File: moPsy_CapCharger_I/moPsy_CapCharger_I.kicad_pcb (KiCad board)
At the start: 2 copper layers, 30 x 31 mm, 12 parts, among them J1 Conn_01x08_Male, U1 LM79L12_TO92, U2 LM555xN

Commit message: Add OSHW logo to Cap Charger PCB
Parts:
- added REF**: OSHW-Logo2_7.3x6mm_SilkScreen, Symbol:OSHW-Logo2_7.3x6mm_SilkScreen, B.Cu at (104.8, 67.3)

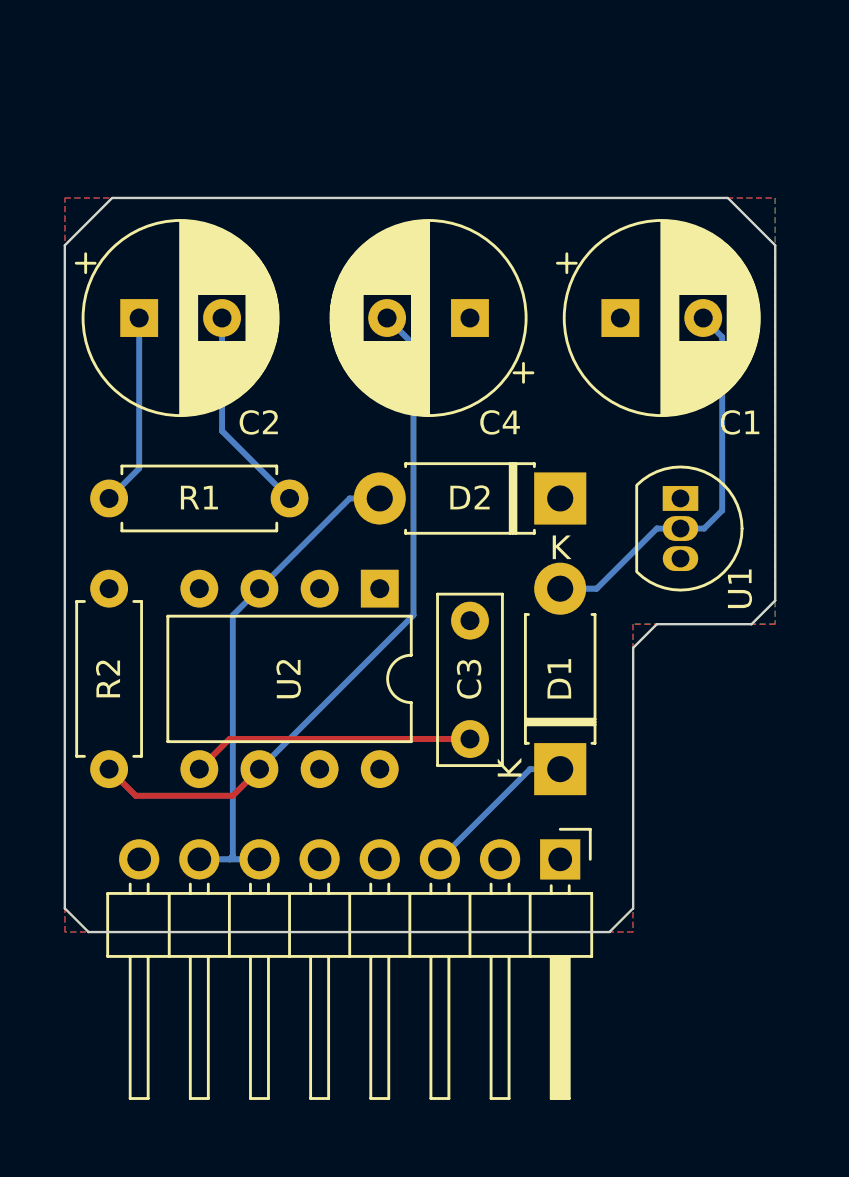
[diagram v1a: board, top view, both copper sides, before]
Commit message: Design a new PCB for the cap charger
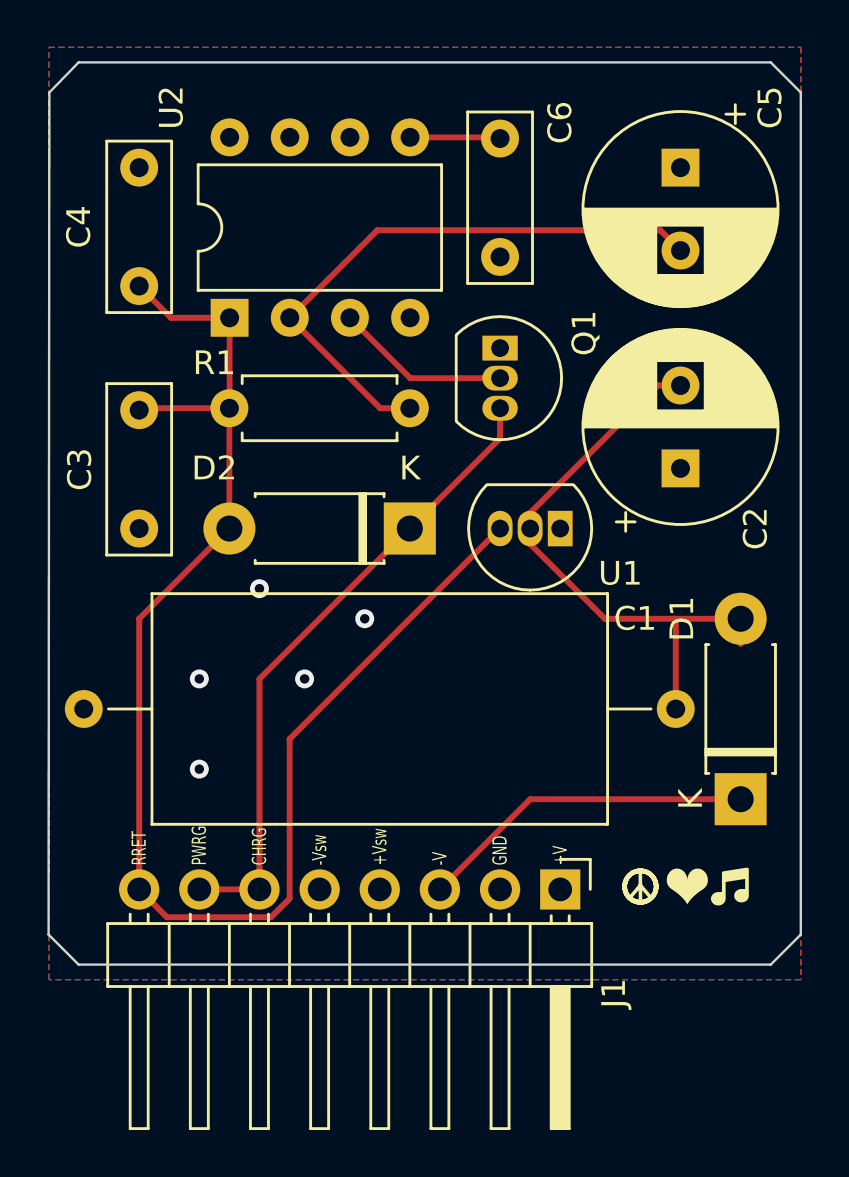
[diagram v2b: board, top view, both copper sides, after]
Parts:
- removed R2: 47k, Resistor_THT:R_Axial_DIN0207_L6.3mm_D2.5mm_P7.62mm_Horizontal
- removed REF**: OSHW-Logo2_7.3x6mm_SilkScreen, Symbol:OSHW-Logo2_7.3x6mm_SilkScreen
- added C5: 100u, Capacitor_THT:CP_Radial_D8.0mm_P3.50mm, F.Cu at (127.0, 45.7)
- added C6: 10n, Capacitor_THT:C_Rect_L7.0mm_W2.5mm_P5.00mm, F.Cu at (119.4, 49.5)
- added Q1: BC547, Package_TO_SOT_THT:TO-92_Inline, F.Cu at (119.4, 53.3)
- C1: value 33u -> 470u; footprint Capacitor_THT:CP_Radial_D8.0mm_P3.50mm -> Capacitor_THT:C_Axial_L19.0mm_D9.5mm_P25.00mm_Horizontal
- C2: value 100n -> 33u
- C3: value 10n -> 100n
- C4: value 100u -> 100n; footprint Capacitor_THT:CP_Radial_D8.0mm_P3.50mm -> Capacitor_THT:C_Rect_L7.0mm_W2.5mm_P5.00mm
- R1: value 10k -> 47k
- moved C1 28.0 mm to (101.8, 68.6)
- moved C2 23.7 mm to (127.0, 58.4), turned to 90 degrees
- moved C3 16.6 mm to (104.1, 61.0)
- moved C4 15.3 mm to (104.1, 45.7), turned to -90 degrees
- moved Ref** 13.8 mm to (113.7, 68.6)
- moved R1 13.3 mm to (115.6, 55.9), turned to 180 degrees
- moved U2 13.1 mm to (108.0, 52.1), turned to 90 degrees
- moved D1 7.73 mm to (129.5, 72.4)
- moved D2 6.48 mm to (115.6, 61.0)
- moved U1 5.24 mm to (121.9, 61.0), turned to 180 degrees
- moved J1 1.27 mm to (121.9, 76.2)
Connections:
- C1 pad 1: REL_RETURN -> GND
- C1 pad 2: Net-(C1-Pad2) -> Net-(C2-Pad2)
- C2 pad 1: REL_RETURN -> GND
- C2 pad 2: -12V -> Net-(C2-Pad2)
- C3 pad 1: Net-(C3-Pad1) -> GND
- C3 pad 2: -12V -> REL_RETURN
- C4 pad 1: REL_RETURN -> GND
- C4 pad 2: Net-(C4-Pad2) -> REL_RETURN
- D1 pad 2: Net-(C1-Pad2) -> Net-(C2-Pad2)
- D2 pad 1: REL_RETURN -> REL_Charge
- D2 pad 2: REL_Charge -> REL_RETURN
- J1 pad 1: (no net) -> +15V
- J1 pad 2: REL_RETURN -> GND
- J1 pad 4: (no net) -> +15V_SW
- J1 pad 5: (no net) -> -15V_SW
- R1 pad 1: REL_RETURN -> Net-(C5-Pad2)
- R1 pad 2: -12V -> REL_RETURN
- U1 pad 1: REL_RETURN -> GND
- U1 pad 2: Net-(C1-Pad2) -> Net-(C2-Pad2)
- U1 pad 3: -12V -> REL_RETURN
- U2 pad 1: -12V -> REL_RETURN
- U2 pad 2: -12V -> Net-(C5-Pad2)
- U2 pad 3: REL_Charge -> Net-(U2-Pad3)
- U2 pad 4: REL_RETURN -> GND
- U2 pad 5: Net-(C3-Pad1) -> Net-(U2-Pad5)
- U2 pad 6: Net-(C4-Pad2) -> unconnected-(U2-Pad6)
- U2 pad 7: (no net) -> unconnected-(U2-Pad7)
- U2 pad 8: REL_RETURN -> GND
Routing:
- net REL_RETURN: track 8.15 -> 60.4 mm
- net Net-(C4-Pad2): track 29.5 -> 0.00 mm
- net Net-(C5-Pad2): track 0.00 -> 25.0 mm
- net Net-(C2-Pad2): track 0.00 -> 25.0 mm
- net Net-(C1-Pad2): track 16.7 -> 0.00 mm
- net Net-(C3-Pad1): track 12.0 -> 0.00 mm
- net -12V: track 8.80 -> 0.00 mm
- net -15V: track 6.66 -> 14.3 mm
- net Net-(U2-Pad3): track 0.00 -> 7.40 mm
- net REL_Charge: track 21.2 -> 27.1 mm
- net Net-(U2-Pad5): track 0.00 -> 3.82 mm
- net GND: vias 0 -> 5
- added copper zone on B.Cu, net GND
- added copper zone on F.Cu, net GND
- removed copper zone on F.Cu, net -12V
- removed copper zone on B.Cu, net REL_RETURN
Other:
- board size 30 x 31 mm -> 31.8 x 38.1 mm
- board text added: "+V"
- board text added: "+Vsw"
- board text added: "-V"
- board text added: "-Vsw"
- board text added: "CC BY-SA 4.0"
- board text added: "CHRG"
- board text added: "GND"
- board text added: "PWRG"
- board text added: "RRET"
- board text added: "Stefan Haun"
- board text added: "https://github.com/moPsy-project/moPsy-PSU"
- board text removed: "moPsy Cap Charger 1"

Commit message: Add fix for delay circuit
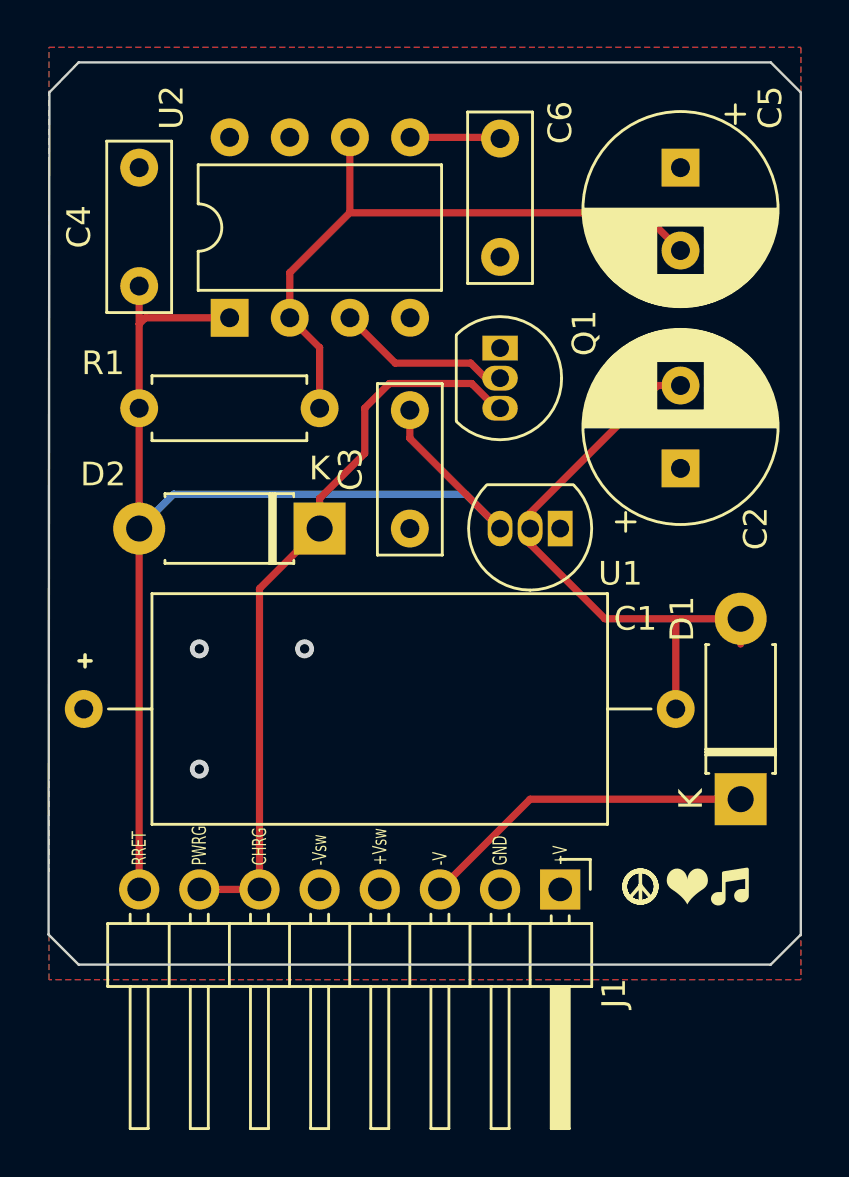
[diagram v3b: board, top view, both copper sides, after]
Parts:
- removed Ref**: Val**, moPsy_KiCad:moPsy_logo_kicad_20x09_FSilk
- moved C3 11.4 mm to (115.6, 61.0)
- moved D2 3.81 mm to (111.8, 61.0)
- moved R1 3.81 mm to (111.8, 55.9)
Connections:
- U2 pad 6: unconnected-(U2-Pad6) -> Net-(C5-Pad2)
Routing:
- net REL_RETURN: track 60.4 -> 52.4 mm
- net REL_Charge: track 27.1 -> 31.3 mm
- net Net-(C5-Pad2): track 25.0 -> 27.6 mm
- net GND: vias 5 -> 3
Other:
- board text added: "PSU Cap Charger v2"

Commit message: Change revision number to 1.1
While it has been a complete re-design, it is effectively still the feature
set from version 1, so only change the minor version.
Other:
- board text added: "PSU Cap Charger v1.1"
- board text removed: "PSU Cap Charger v2"
